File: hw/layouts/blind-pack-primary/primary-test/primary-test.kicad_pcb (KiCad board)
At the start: 2 copper layers, 50 parts

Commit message: Publish complete controller schematic and retained carrier placements
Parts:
- added H1: M3 clearance 3.4 mm, blind-pack-features:MountingHole_M3_3.4mm, F.Cu at (104.0, 200.0)
- added H2: M3 clearance 3.4 mm, blind-pack-features:MountingHole_M3_3.4mm, F.Cu at (182.0, 200.0)
- added H3: M3 clearance 3.4 mm, blind-pack-features:MountingHole_M3_3.4mm, F.Cu at (104.0, 104.0)
- added H4: M3 clearance 3.4 mm, blind-pack-features:MountingHole_M3_3.4mm, F.Cu at (182.0, 104.0)
- moved TP3 367.3 mm to (137.7, 104.0)
- moved TP1 357.2 mm to (130.0, 109.5)
- moved TP2 342.0 mm to (126.0, 109.5)
- moved TP16 336.3 mm to (122.0, 109.5)
- moved TP17 330.7 mm to (118.0, 109.5)
- moved TP14 325.0 mm to (114.0, 109.5)
- moved TP4 322.1 mm to (177.0, 109.2)
- moved TP15 319.4 mm to (110.0, 109.5)
- moved TP5 308.9 mm to (171.0, 109.2)
- moved TP6 259.1 mm to (165.0, 109.2)
- moved TP7 255.5 mm to (159.0, 109.2)
- moved TP8 251.9 mm to (153.0, 109.2)
- moved TP9 248.3 mm to (147.0, 109.2)
- moved C4 241.6 mm to (151.0, 197.6), turned to 90 degrees
- moved R8 241.6 mm to (161.0, 197.6), turned to 90 degrees
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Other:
- board outline added: 86 x 104 mm

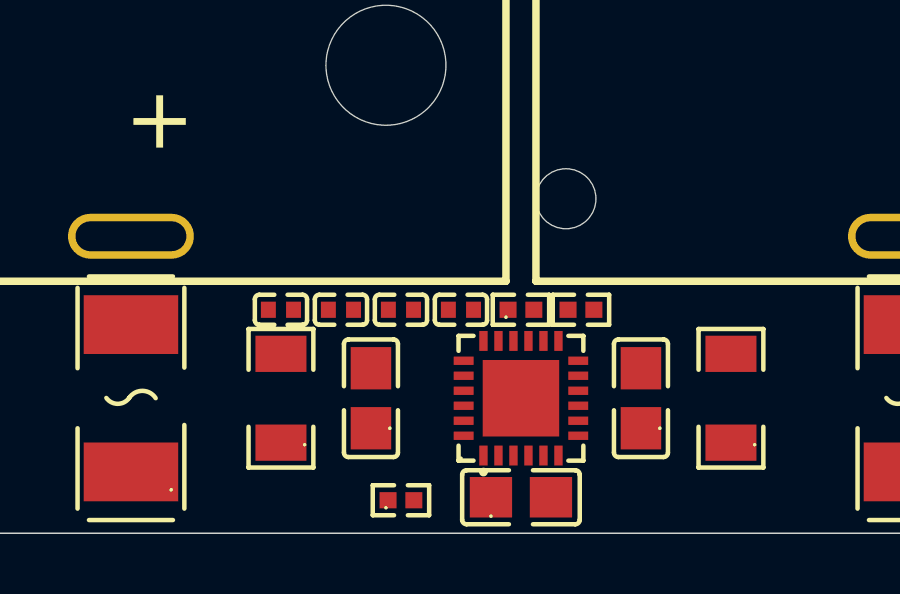
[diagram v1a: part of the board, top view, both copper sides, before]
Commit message: Coordinate retained enclosure and PCB clearance repair checkpoint
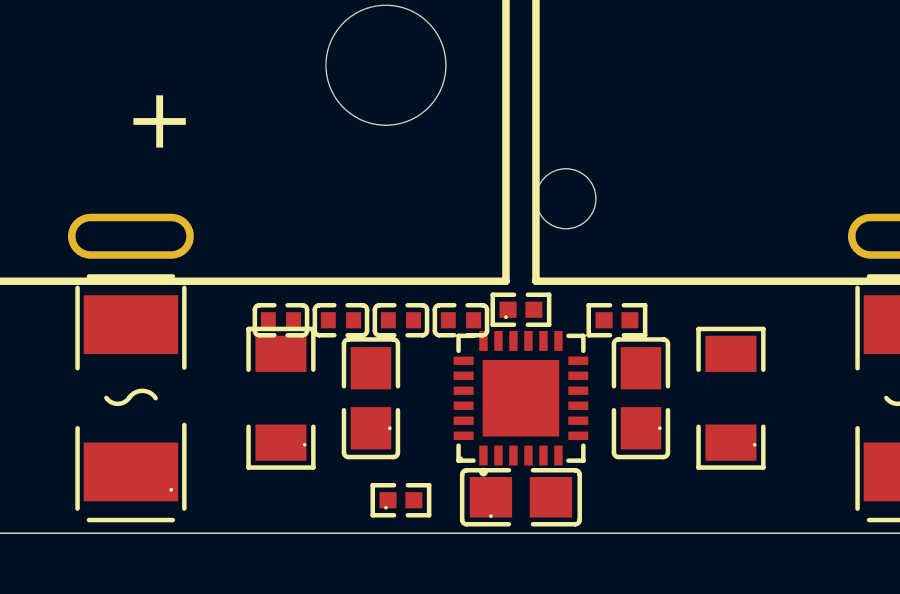
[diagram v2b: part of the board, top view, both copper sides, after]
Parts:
- moved R2 1.25 mm to (131.2, 196.9)
- moved C1 0.35 mm to (120.0, 196.9)
- moved C2 0.35 mm to (122.0, 196.9)
- moved C3 0.35 mm to (124.0, 196.9)
- moved C8 0.35 mm to (126.0, 196.9)

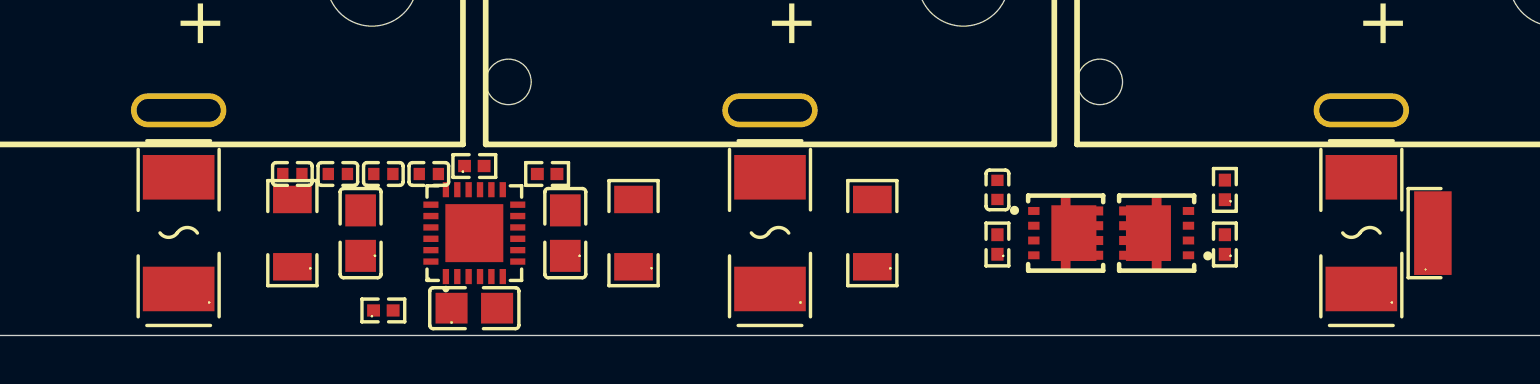
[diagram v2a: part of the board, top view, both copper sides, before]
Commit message: Fix inherited package clearances and repack all three boards
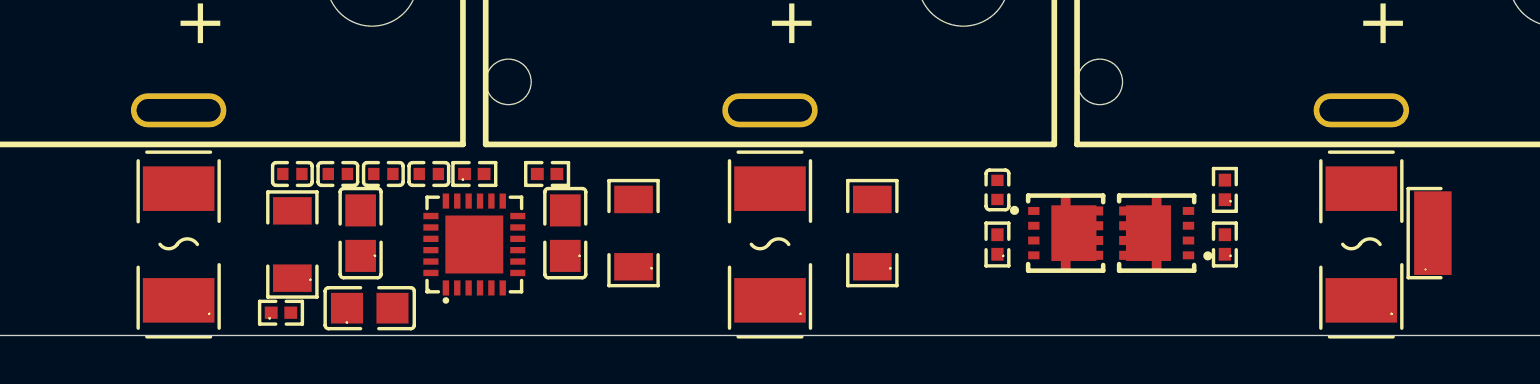
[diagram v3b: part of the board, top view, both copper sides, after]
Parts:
- moved C7 4.60 mm to (123.4, 202.8)
- moved R12 4.50 mm to (119.5, 203.0)
- moved F1 0.50 mm to (115.0, 200.0)
- moved F2 0.50 mm to (141.0, 200.0)
- moved F3 0.50 mm to (167.0, 200.0)
- moved R3 0.50 mm to (120.0, 200.0)
- moved U1 0.50 mm to (128.0, 200.0)
- moved R9 0.35 mm to (128.0, 196.9)

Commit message: Connect primary battery routing and correct communication protection
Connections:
- BT1 pad 2: 2 -> carrier-contact-1
- C1 pad 1: carrier.protection-2 -> 2
- C1 pad 2: 2 -> carrier-contact-1
- C2 pad 1: carrier.protection-2-1 -> carrier.protection-2
- C2 pad 2: carrier.protection-2 -> 2
- C3 pad 2: carrier.protection-2-1 -> carrier.protection-2
- C6 pad 2: 2 -> carrier-contact-1
- C7 pad 2: 2 -> carrier-contact-1
- C8 pad 2: 2 -> carrier-contact-1
- D1 pad 1: ALRT -> carrier-1-2
- D1 pad 2: 2 -> lv
- D2 pad 1: K -> carrier-1-3
- D2 pad 2: 2 -> lv
- D3 pad 1: carrier.protection-K -> carrier-1-4
- D3 pad 2: 2 -> lv
- R1 pad 1: alert_n -> carrier-1-2
- R10 pad 1: carrier-contact-1 -> carrier-1-3
- R10 pad 2: K -> SCL_DOD
- R11 pad 1: carrier-contact-2 -> carrier-1-4
- R11 pad 2: carrier.protection-K -> SDA_DQ
- R13 pad 1: 2 -> carrier-contact-1
- R2 pad 2: 2 -> carrier-contact-1
- R3 pad 2: carrier.protection-2 -> 2
- R4 pad 2: carrier.protection-2-1 -> carrier.protection-2
- R9 pad 2: 2 -> carrier-contact-1
- TP12 pad 1: 2 -> carrier-contact-1
- TP14 pad 1: 2 -> carrier-contact-1
- TP15 pad 1: carrier-contact-3 -> carrier-contact-2
- TP16 pad 1: 2 -> carrier-contact-1
- TP17 pad 1: carrier-contact-4 -> carrier-contact-3
- TP3 pad 1: alert_n -> carrier-1-2
- TP6 pad 1: carrier-contact-1 -> carrier-1-3
- TP7 pad 1: carrier-contact-2 -> carrier-1-4
- U1 pad 10: carrier-contact-3 -> carrier-contact-2
- U1 pad 15: 2 -> carrier-contact-1
- U1 pad 16: carrier-contact-4 -> carrier-contact-3
- U1 pad 18: 2 -> carrier-contact-1
- U1 pad 19: 2 -> carrier-contact-1
- U1 pad 20: 2 -> carrier-contact-1
- U1 pad 21: carrier.protection-2 -> 2
- U1 pad 22: carrier.protection-2 -> 2
- U1 pad 23: carrier.protection-2-1 -> carrier.protection-2
- U1 pad 25: 2 -> carrier-contact-1
- U1 pad 8: K -> SCL_DOD
- U1 pad 9: carrier.protection-K -> SDA_DQ
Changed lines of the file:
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@@
   (net 3 "1")
   (net 4 "carrier-1")
-  (net 5 "alert_n")
-  (net 6 "carrier-contact-1")
-  (net 7 "carrier-contact-2")
   (net 8 "hv")
   (net 9 "carrier-1-1")
   (net 10 "junction1")
-  (net 11 "carrier-contact-3")
-  (net 12 "carrier-contact-4")
-  (net 13 "carrier.protection-2-1")
+  (net 11 "carrier-contact-2")
+  (net 12 "carrier-contact-3")
+  (net 13 "carrier.protection-2")
   (net 14 "carrier.protection-1-1")
   (net 15 "carrier.protection-1-2")
-  (net 16 "2")
+  (net 16 "carrier-contact-1")
   (net 17 "raw_top")
   (net 18 "G")
@@
   (net 20 "carrier.protection-1")
   (net 21 "AOLDO")
-  (net 22 "lv")
   (net 23 "CP")
   (net 24 "BATTS")
@@
   (net 27 "ZVC")
   (net 28 "PCKP")
-  (net 29 "carrier.protection-2")
+  (net 29 "2")
   (net 30 "junction2")
   (net 31 "carrier.protection-G")
   (net 32 "PFAIL")
   (net 33 "ALRT")
-  (net 34 "K")
-  (net 35 "carrier.protection-K")
+  (net 34 "SCL_DOD")
+  (net 35 "SDA_DQ")
+  (net 36 "carrier-1-2")
+  (net 37 "carrier-1-4")
+  (net 38 "lv")
+  (net 39 "carrier-1-3")
   (footprint
     "blind-carrier:FUSE-SMD_L6.1-W2.7"
@@
       (drill 1.2)
       (layers "*.Cu" "*.Mask")
-      (net 5 "alert_n")
+      (net 36 "carrier-1-2")
 ))
   (footprint
@@
       (size 0.665 0.28)
       (layers "F.Cu" "F.Mask" "F.Paste")
-      (net 34 "K")
+      (net 34 "SCL_DOD")
 )
     (pad
@@
       (size 0.665 0.28)
       (layers "F.Cu" "F.Mask" "F.Paste")
-      (net 35 "carrier.protection-K")
+      (net 35 "SDA_DQ")
 )
     (pad
@@
       (size 0.665 0.28)
       (layers "F.Cu" "F.Mask" "F.Paste")
-      (net 11 "carrier-contact-3")
+      (net 11 "carrier-contact-2")
 )
     (pad
@@
       (size 0.28 0.665)
       (layers "F.Cu" "F.Mask" "F.Paste")
-      (net 22 "lv")
+      (net 38 "lv")
 )
     (pad
@@
       (size 0.28 0.665)
       (layers "F.Cu" "F.Mask" "F.Paste")
-      (net 16 "2")
+      (net 16 "carrier-contact-1")
 )
     (pad
@@
       (size 0.28 0.665)
       (layers "F.Cu" "F.Mask" "F.Paste")
-      (net 12 "carrier-contact-4")
+      (net 12 "carrier-contact-3")
 )
     (pad
@@
       (size 0.28 0.665)
       (layers "F.Cu" "F.Mask" "F.Paste")
-      (net 16 "2")
+      (net 16 "carrier-contact-1")
 )
     (pad
@@
       (size 0.665 0.28)
       (layers "F.Cu" "F.Mask" "F.Paste")
-      (net 16 "2")
+      (net 16 "carrier-contact-1")
 )
     (pad
@@
       (size 0.665 0.28)
       (layers "F.Cu" "F.Mask" "F.Paste")
-      (net 16 "2")
+      (net 16 "carrier-contact-1")
 )
     (pad
@@
       (size 0.665 0.28)
       (layers "F.Cu" "F.Mask" "F.Paste")
-      (net 29 "carrier.protection-2")
+      (net 29 "2")
 )
     (pad
@@
       (size 0.665 0.28)
       (layers "F.Cu" "F.Mask" "F.Paste")
-      (net 29 "carrier.protection-2")
+      (net 29 "2")
 )
     (pad
@@
       (size 0.665 0.28)
       (layers "F.Cu" "F.Mask" "F.Paste")
-      (net 13 "carrier.protection-2-1")
+      (net 13 "carrier.protection-2")
 )
     (pad
@@
       (size 2.55 2.55)
       (layers "F.Cu" "F.Mask" "F.Paste")
-      (net 16 "2")
+      (net 16 "carrier-contact-1")
 )
     (embedded_fonts no)
@@
       (drill 1.2)
       (layers "*.Cu" "*.Mask")
-      (net 16 "2")
+      (net 16 "carrier-contact-1")
 ))
   (footprint
@@
       (size 0.5 0.54)
       (layers "F.Cu" "F.Paste" "F.Mask")
-      (net 13 "carrier.protection-2-1")
+      (net 13 "carrier.protection-2")
 )
     (pad
@@
       (size 0.5 0.54)
       (layers "F.Cu" "F.Paste" "F.Mask")
-      (net 29 "carrier.protection-2")
+      (net 29 "2")
 )
     (embedded_fonts no)
@@
       (size 0.566 0.54)
       (layers "F.Cu" "F.Mask" "F.Paste")
-      (net 16 "2")
+      (net 16 "carrier-contact-1")
 )
     (embedded_fonts no)
@@
       (drill 1.2)
       (layers "*.Cu" "*.Mask")
-      (net 16 "2")
+      (net 16 "carrier-contact-1")
 ))
   (footprint
@@
       (size 0.566 0.54)
       (layers "F.Cu" "F.Mask" "F.Paste")
-      (net 7 "carrier-contact-2")
+      (net 37 "carrier-1-4")
 )
     (pad
@@
       (size 0.566 0.54)
       (layers "F.Cu" "F.Mask" "F.Paste")
-      (net 35 "carrier.protection-K")
+      (net 35 "SDA_DQ")
 )
     (embedded_fonts no)
@@
       (size 1.208 1.701)
       (layers "F.Cu" "F.Mask" "F.Paste")
-      (net 29 "carrier.protection-2")
+      (net 29 "2")
 )
     (embedded_fonts no)
@@
       (size 0.5 0.54)
       (layers "F.Cu" "F.Paste" "F.Mask")
-      (net 13 "carrier.protection-2-1")
+      (net 13 "carrier.protection-2")
 )
     (embedded_fonts no)
@@
       (size 0.57 0.54)
       (layers "F.Cu" "F.Paste" "F.Mask")
-      (net 16 "2")
+      (net 16 "carrier-contact-1")
 )
     (embedded_fonts no)
@@
       (size 0.95 1.15)
       (layers "F.Cu" "F.Mask" "F.Paste")
-      (net 35 "carrier.protection-K")
+      (net 37 "carrier-1-4")
 )
     (pad
@@
       (size 0.95 1.15)
       (layers "F.Cu" "F.Mask" "F.Paste")
-      (net 16 "2")
+      (net 38 "lv")
 )
     (embedded_fonts no)
@@
       (size 0.95 1.15)
       (layers "F.Cu" "F.Mask" "F.Paste")
-      (net 34 "K")
+      (net 39 "carrier-1-3")
 )
     (pad
@@
       (size 0.95 1.15)
       (layers "F.Cu" "F.Mask" "F.Paste")
-      (net 16 "2")
+      (net 38 "lv")
 )
     (embedded_fonts no)
@@
       (drill 1.5)
       (layers "*.Cu" "*.Mask")
-      (net 22 "lv")
+      (net 38 "lv")
 ))
   (footprint
@@
       (drill 1.2)
       (layers "*.Cu" "*.Mask")
-      (net 12 "carrier-contact-4")
+      (net 12 "carrier-contact-3")
 ))
   (footprint
@@
       (size 0.566 0.54)
       (layers "F.Cu" "F.Mask" "F.Paste")
-      (net 5 "alert_n")
+      (net 36 "carrier-1-2")
 )
     (pad
@@
       (size 1.41 1.35)
       (layers "F.Cu" "F.Mask" "F.Paste")
-      (net 16 "2")
+      (net 16 "carrier-contact-1")
 )
     (embedded_fonts no)
@@
       (size 0.5 0.54)
       (layers "F.Cu" "F.Paste" "F.Mask")
-      (net 29 "carrier.protection-2")
+      (net 29 "2")
 )
     (pad
@@
       (size 0.5 0.54)
       (layers "F.Cu" "F.Paste" "F.Mask")
-      (net 16 "2")
+      (net 16 "carrier-contact-1")
 )
     (embedded_fonts no)
@@
       (drill 1.5)
       (layers "*.Cu" "*.Mask")
-      (net 16 "2")
+      (net 16 "carrier-contact-1")
 ))
   (footprint
@@
       (size 0.95 1.15)
       (layers "F.Cu" "F.Mask" "F.Paste")
-      (net 33 "ALRT")
+      (net 36 "carrier-1-2")
 )
     (pad
@@
       (size 0.95 1.15)
       (layers "F.Cu" "F.Mask" "F.Paste")
-      (net 16 "2")
+      (net 38 "lv")
 )
     (embedded_fonts no)
@@
       (drill 1.5)
       (layers "*.Cu" "*.Mask")
-      (net 7 "carrier-contact-2")
+      (net 37 "carrier-1-4")
 ))
   (footprint
@@
       (size 0.566 0.54)
       (layers "F.Cu" "F.Mask" "F.Paste")
-      (net 6 "carrier-contact-1")
+      (net 39 "carrier-1-3")
 )
     (pad
@@
       (size 0.566 0.54)
       (layers "F.Cu" "F.Mask" "F.Paste")
-      (net 34 "K")
+      (net 34 "SCL_DOD")
 )
     (embedded_fonts no)
@@
       (drill 1.2)
       (layers "*.Cu" "*.Mask")
-      (net 11 "carrier-contact-3")
+      (net 11 "carrier-contact-2")
 ))
   (footprint
@@
       (size 0.5 0.54)
       (layers "F.Cu" "F.Paste" "F.Mask")
-      (net 16 "2")
+      (net 16 "carrier-contact-1")
 )
     (embedded_fonts no)
@@
       (drill 1.5)
       (layers "*.Cu" "*.Mask")
-      (net 6 "carrier-contact-1")
+      (net 39 "carrier-1-3")
 ))
   (footprint
@@
       (size 1.65 3.68)
       (layers "F.Cu" "F.Mask" "F.Paste")
-      (net 16 "2")
+      (net 16 "carrier-contact-1")
 )
     (pad
@@
       (size 1.65 3.68)
       (layers "F.Cu" "F.Mask" "F.Paste")
-      (net 22 "lv")
+      (net 38 "lv")
 )
     (embedded_fonts no)
@@
       (size 1.41 1.35)
       (layers "F.Cu" "F.Mask" "F.Paste")
-      (net 16 "2")
+      (net 16 "carrier-contact-1")
 )
     (embedded_fonts no)
@@
       (layers "*.Cu" "*.Mask")
       (remove_unused_layers no)
-      (net 16 "2")
+      (net 16 "carrier-contact-1")
 )
     (embedded_fonts no)
@@
       (size 1.208 1.701)
       (layers "F.Cu" "F.Mask" "F.Paste")
-      (net 13 "carrier.protection-2-1")
+      (net 13 "carrier.protection-2")
 )
     (embedded_fonts no)
